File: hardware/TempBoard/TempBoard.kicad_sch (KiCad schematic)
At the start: 17 parts, among them J1 Conn_01x04, J2 Conn_01x03, U1 BME280

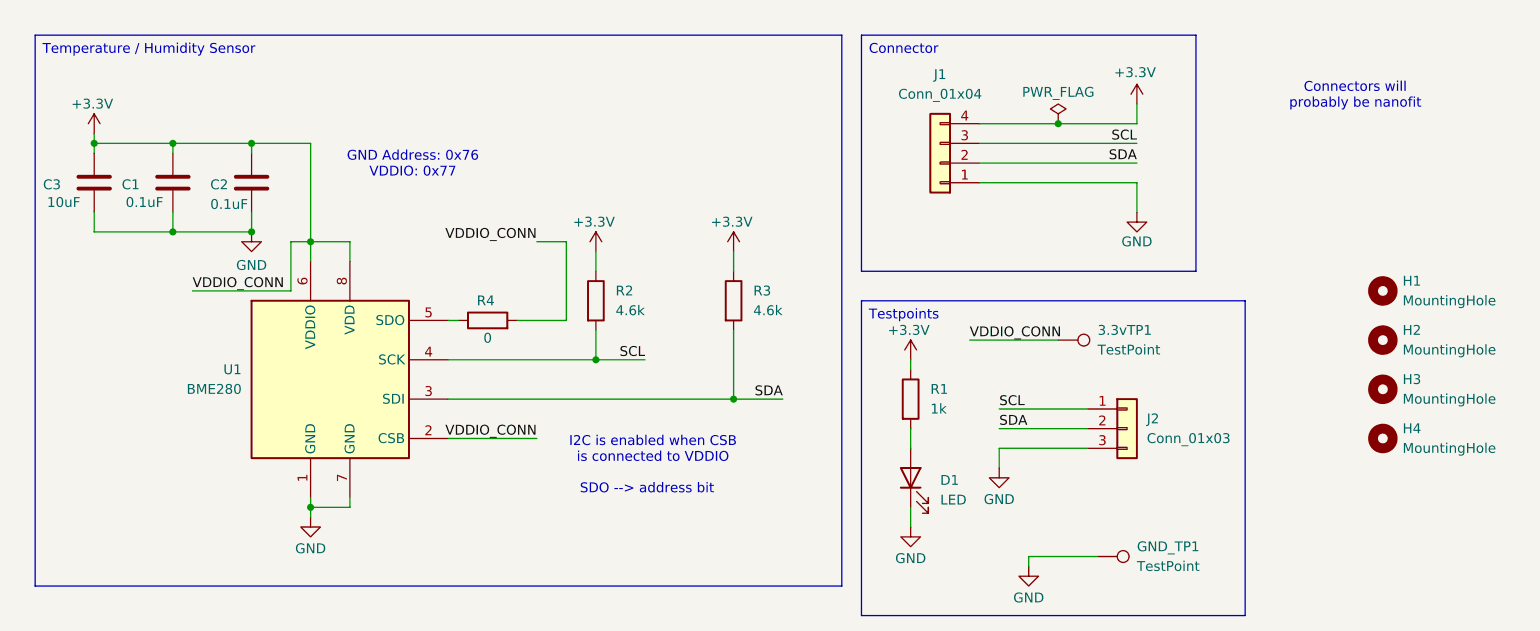
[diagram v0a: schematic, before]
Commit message: Pitot Board Rev B (#3)
* init

* added layout

* ready to review

* finished pitot board

* pitot board ordered, routing+size finished for temperature board so pull??

* finished tempboard silkscreen

* resized temperature board

* poo oo ee

* ughhhhhhhhhhhhhhhhhhghghghhhhhhhhhhhhhhhhhhh

* working i2c on RH board

* cleanup?

* small

* added read me

* fixed mistake

* Fix image filename case in README.md

* Add new line for telemetry components explanation
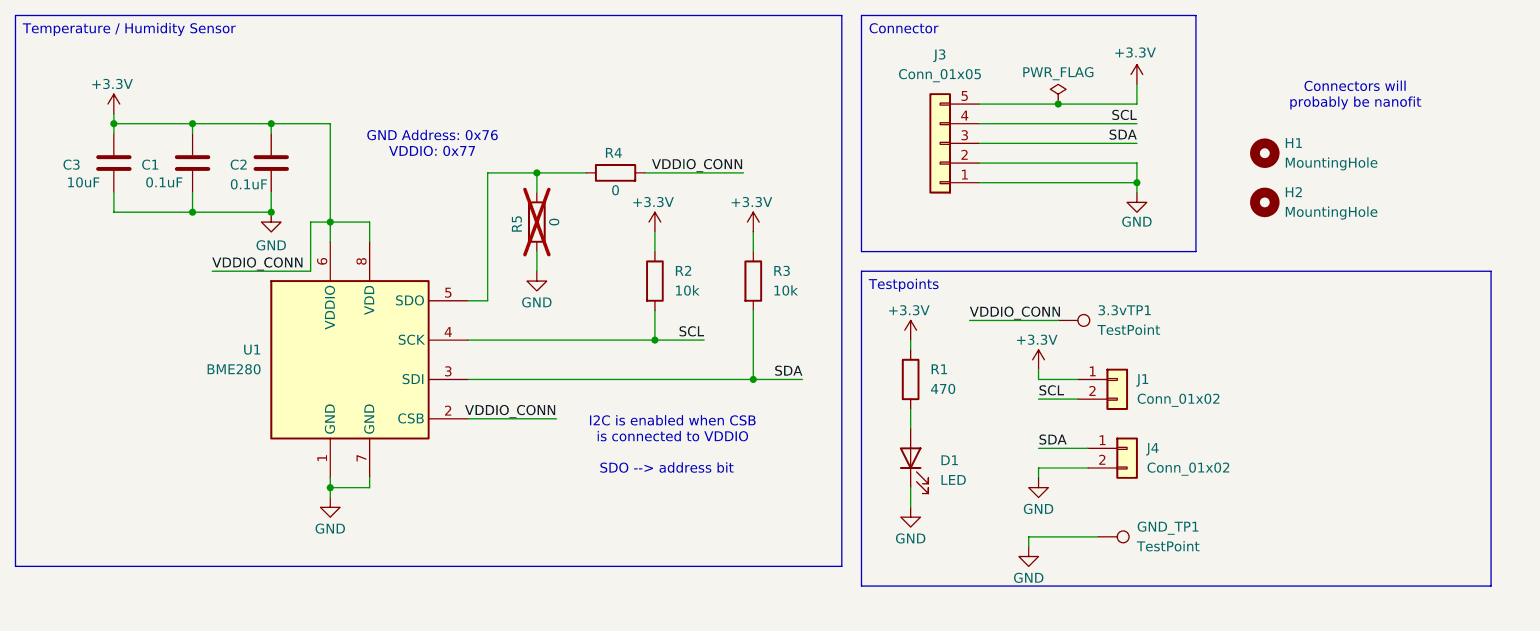
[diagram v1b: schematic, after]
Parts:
- removed H3, H4: MountingHole, MountingHole:MountingHole_3.2mm_M3, symbol Mechanical:MountingHole
- removed J1: Conn_01x04, Connector_Molex:Molex_Nano-Fit_105313-xx04_1x04_P2.50mm_Horizontal, symbol Connector_Generic:Conn_01x04
- removed J2: Conn_01x03, Connector_PinHeader_2.54mm:PinHeader_1x03_P2.54mm_Vertical, symbol Connector_Generic:Conn_01x03
- added J1, J4: Conn_01x02, Connector_PinHeader_2.54mm:PinHeader_1x02_P2.54mm_Vertical, symbol Connector_Generic:Conn_01x02
- added J3: Conn_01x05, Connector_Molex:Molex_Nano-Fit_105313-xx05_1x05_P2.50mm_Horizontal, symbol Connector_Generic:Conn_01x05
- added R5: 0, Resistor_SMD:R_0603_1608Metric_Pad0.98x0.95mm_HandSolder, symbol Device:R
- 3.3vTP1, GND_TP1: footprint TestPoint:TestPoint_Pad_1.0x1.0mm -> TestPoint:TestPoint_THTPad_1.0x1.0mm_Drill0.5mm
- C3: footprint Capacitor_SMD:C_0603_1608Metric_Pad1.08x0.95mm_HandSolder -> Capacitor_SMD:C_0805_2012Metric_Pad1.18x1.45mm_HandSolder
- R1: value 1k -> 470
- R2, R3: value 4.6k -> 10k
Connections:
- net +3.3V: now also J1.1 (Pin_1), J3.5 (Pin_5)
- net GND: now also J3.1 (Pin_1), J3.2 (Pin_2), J4.2 (Pin_2), R5.1
- net SCL: now also J1.2 (Pin_2), J3.4 (Pin_4)
- net SDA: now also J3.3 (Pin_3), J4.1 (Pin_1)
- net at R4.1, U1.5 (SDO): now also R5.2
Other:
- moved on the sheet: 3.3vTP1, C1, C2, C3, D1, GND_TP1, H1, H2, R1, R2, R3, R4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
